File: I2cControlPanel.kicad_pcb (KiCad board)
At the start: 2 copper layers, 100 x 100 mm, 54 parts, among them J1 JoystickL, J2 Conn_01x06, J3 Conn_01x04, J4 Conn_01x04, J5 JoystickR, J6 Conn_01x04, SW6 SW_Push, U1 NJM12888F33, U2 ATmega328PB-MU, U3 AQM0802

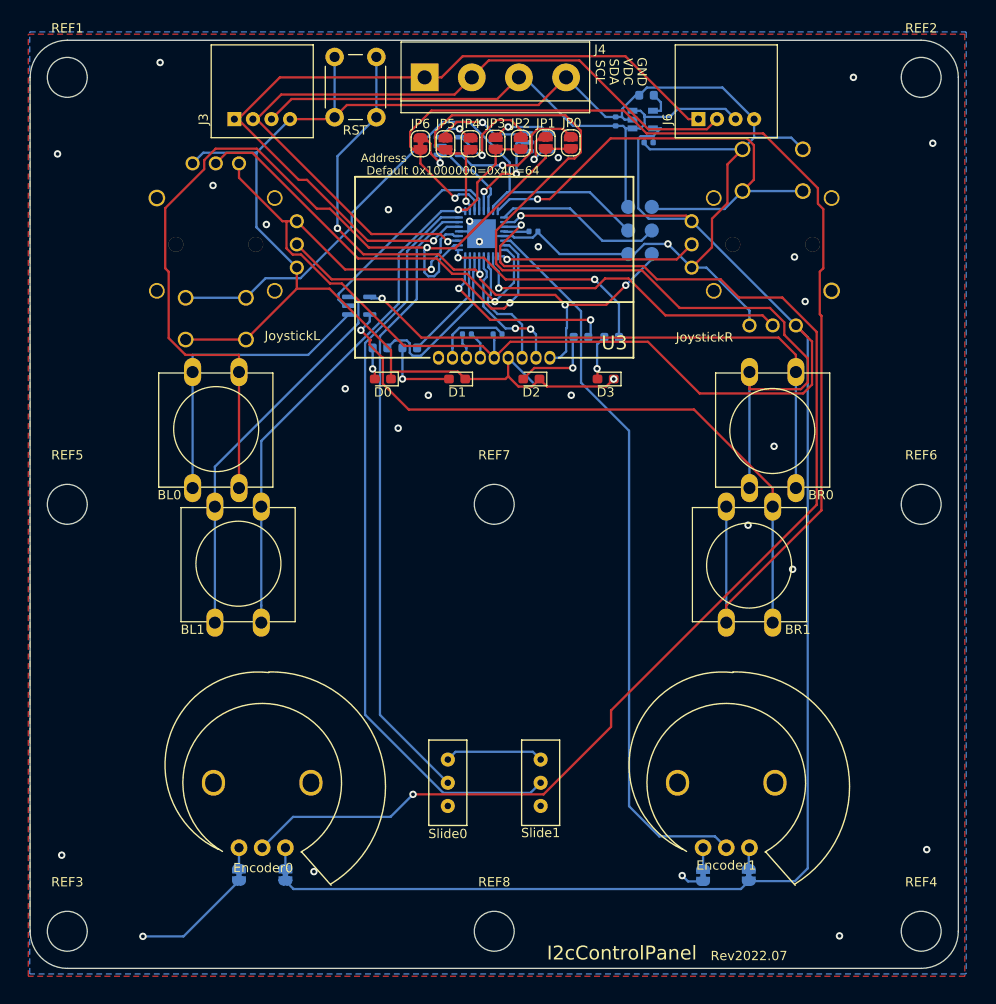
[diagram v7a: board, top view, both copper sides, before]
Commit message: Add A package for ATmega328PB
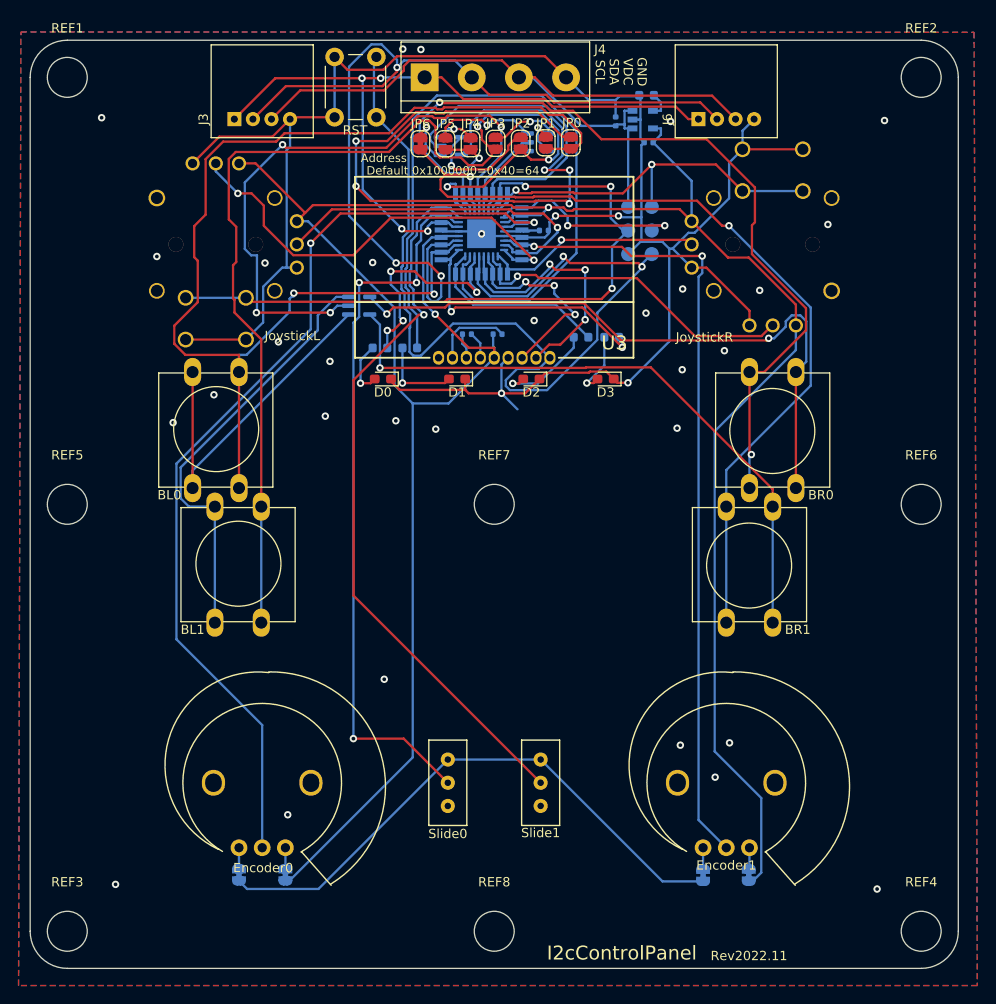
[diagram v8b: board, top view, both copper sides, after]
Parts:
- added U4: ATmega328PB-A, asukiaaa-kicad-footprints:TQFP-32_7x7mm_P0.8mm_short_inner, B.Cu at (98.6, 70.8)
- moved C4 1.12 mm to (105.3, 70.5)
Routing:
- net Net-(D4-Pad5): track 15.3 -> 81.4 mm, vias 1 -> 5
- net /LED1: track 12.2 -> 77.8 mm
- net /BTN1: track 66.5 -> 121.4 mm, vias 1 -> 3
- net /BtnSig0: track 23.5 -> 66.9 mm, vias 0 -> 4
- net /RST: track 69.5 -> 106.5 mm, vias 4 -> 2
- net GND: track 255.4 -> 292.0 mm, vias 27 -> 35
- net /Rotery1: track 138.8 -> 104.2 mm
- net /BTN3: track 125.8 -> 95.2 mm, vias 1 -> 2
- net /BTN0: track 101.9 -> 127.3 mm, vias 1 -> 2
- net /BtnSig2: track 10.1 -> 34.4 mm
- net /SDA: track 83.4 -> 104.9 mm, vias 1 -> 3
- net VDC: track 66.2 -> 81.2 mm
- net /SCL_inside: track 15.1 -> 28.3 mm, vias 2 -> 3
- net /JoyBtnR: track 53.8 -> 41.8 mm, vias 1 -> 2
- net /BTN2: track 110.2 -> 98.9 mm, vias 1 -> 3
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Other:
- board text added: "Rev2022.11"
- board text removed: "Rev2022.07"
